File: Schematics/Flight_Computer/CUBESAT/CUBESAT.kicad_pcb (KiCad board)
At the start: 2 copper layers, 90 x 90 mm, 47 parts, among them J1 6 Pin Connector, J2 M22-6003005, J3 UFL, U1 ADXL345BCCZ, U2 NEO-M8N-0, U3 IAM-20380, U4 MAGNETOMETER, U5 STM32F446RET6, U6 LM75AIM_NOPB

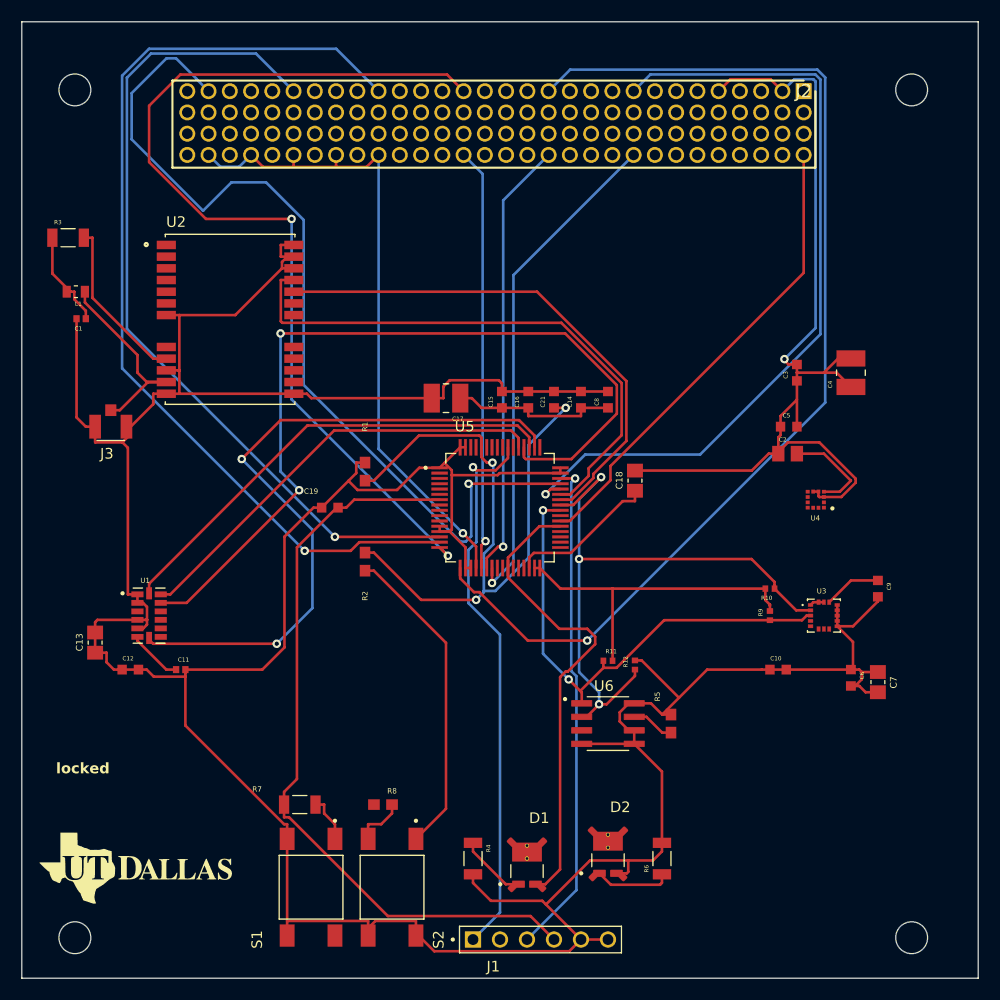
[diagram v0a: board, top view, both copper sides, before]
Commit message: updated pcb without traces or via's
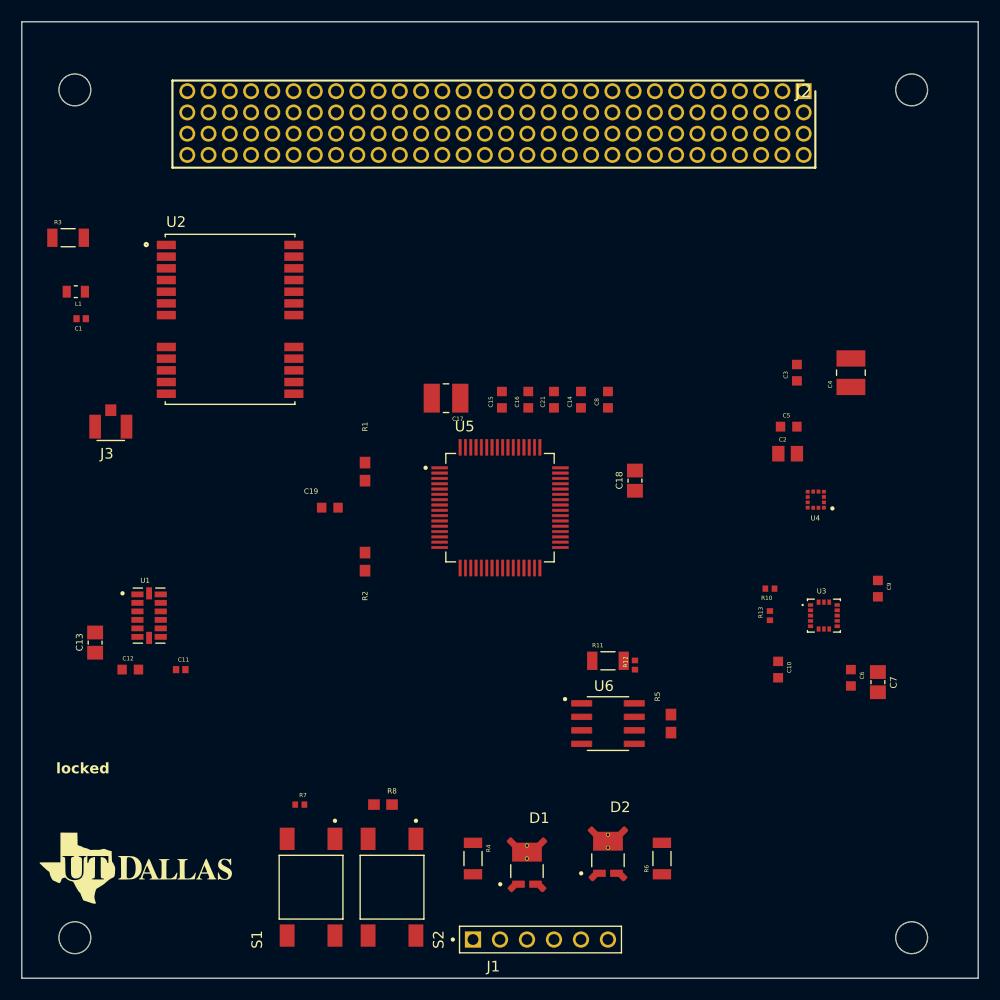
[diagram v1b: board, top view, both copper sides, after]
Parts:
- removed R9: ~, CUBESAT:Resistor4.7kO
- added R13: 4.7k, CUBESAT:Resistor4.7kO, F.Cu at (182.9, 104.1)
- J1: value 6 Pin Connector -> Conn_01x06_Pin
- J3: value UFL -> U.FL-R-SMT_01_
- R11: value 4.7k -> 100; footprint CUBESAT:Resistor4.7kO -> CUBESAT:Reistor100O
- R7: value 100 -> 4.7k; footprint CUBESAT:Reistor100O -> CUBESAT:Resistor4.7kO
- turned C10 to -90 degrees
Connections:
- C1 pad 2: 3.3 V -> GND
- C10 pad 1: 3.3 V -> GND
- C12 pad 2: 3.3 V -> GND
- C13 pad 2: 3.3 V -> GND
- C14 pad 1: Net-(C14-Pad1) -> 3.3 V
- C14 pad 2: 3.3 V -> GND
- C15 pad 1: Net-(C14-Pad1) -> 3.3 V
- C15 pad 2: 3.3 V -> GND
- C16 pad 1: Net-(C14-Pad1) -> 3.3 V
- C16 pad 2: 3.3 V -> GND
- C17 pad 1: Net-(C14-Pad1) -> 3.3 V
- C17 pad 2: 3.3 V -> GND
- C18 pad 1: Net-(U5-VCAP_1) -> GND
- C18 pad 2: 3.3 V -> Net-(U5-VCAP_1)
- C19 pad 2: 3.3 V -> GND
- C2 pad 1: 3.3 V -> GND
- C21 pad 1: BOOT0 -> GND
- C21 pad 2: 3.3 V -> BOOT0
- C3 pad 1: 3.3 V -> GND
- C4 pad 1: 3.3 V -> GND
- C5 pad 1: 3.3 V -> GND
- C6 pad 2: 3.3 V -> GND
- C7 pad 2: 3.3 V -> GND
- C8 pad 1: Net-(C14-Pad1) -> 3.3 V
- C8 pad 2: 3.3 V -> GND
- C9 pad 2: 3.3 V -> GND
- J1 pad 2: unconnected-(J1-Pad2) -> SWCLK
- J1 pad 6: 3.3 V -> GND
- J2 pad 2: 3.3 V -> GND
- J3 pad 1: 3.3 V -> GND
- J3 pad 2: 3.3 V -> GND
- R1 pad 1: 3.3 V -> GND
- R11 pad 1: I2C 3 SDA -> Net-(R11-Pad1)
- R11 pad 2: 3.3 V -> NRST
- R4 pad 2: 3.3 V -> GND
- R5 pad 1: Net-(U6-A0) -> 3.3 V
- R5 pad 2: 3.3 V -> Net-(U6-A0)
- R6 pad 2: 3.3 V -> GND
- R7 pad 1: NRST -> 3.3 V
- R7 pad 2: Net-(R7-Pad2) -> I2C 3 SCL
- R8 pad 1: 3.3 V -> GND
- S1 pad 1: Net-(R7-Pad2) -> Net-(R11-Pad1)
- S1 pad 2: 3.3 V -> GND
- S1 pad 4: 3.3 V -> GND
- S2 pad 4: 3.3 V -> unconnected-(S2-Pad4)
- U1 pad 2: 3.3 V -> GND
- U1 pad 4: 3.3 V -> GND
- U1 pad 5: 3.3 V -> GND
- U2 pad 10: 3.3 V -> GND
- U2 pad 12: 3.3 V -> GND
- U2 pad 13: 3.3 V -> GND
- U2 pad 24: 3.3 V -> GND
- U2 pad 7: 3.3 V -> GND
- U3 pad 10: 3.3 V -> GND
- U3 pad 11: 3.3 V -> GND
- U3 pad 12: 3.3 V -> GND
- U3 pad 13: 3.3 V -> GND
- U3 pad 15: 3.3 V -> GND
- U3 pad 7: 3.3 V -> GND
- U3 pad 9: 3.3 V -> GND
- U4 pad 3: 3.3 V -> GND
- U5 pad 12: 3.3 V -> GND
- U5 pad 18: 3.3 V -> GND
- U5 pad 31: 3.3 V -> GND
- U5 pad 47: 3.3 V -> GND
- U5 pad 63: 3.3 V -> GND
- U6 pad 4: 3.3 V -> GND
- U6 pad 5: 3.3 V -> GND
- U6 pad 6: 3.3 V -> GND
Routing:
- net 3.3 V: track 483.3 -> 0.00 mm, vias 1 -> 0
- net Phase Shifter 2: track 104.8 -> 0.00 mm, vias 1 -> 0
- net Phase Shifter 4: track 91.7 -> 0.00 mm, vias 1 -> 0
- net Phase Shifter 3: track 91.3 -> 0.00 mm, vias 2 -> 0
- net TRX: track 87.1 -> 0.00 mm, vias 1 -> 0
- net ADXL345 MISO: track 80.8 -> 0.00 mm, vias 2 -> 0
- net MODEM RESET: track 79.3 -> 0.00 mm, vias 1 -> 0
- net Phase Shifter 1: track 76.1 -> 0.00 mm, vias 1 -> 0
- net NRST: track 71.3 -> 0.00 mm
- net ADXL345 CS: track 64.6 -> 0.00 mm, vias 2 -> 0
- net BOOT0: track 64.0 -> 0.00 mm, vias 3 -> 0
- net CC1120 (NSS/CS): track 62.8 -> 0.00 mm, vias 1 -> 0
- net I2C 3 SCL: track 59.3 -> 0.00 mm, vias 3 -> 0
- net NEO-M8N-0 RXD: track 53.0 -> 0.00 mm
- net SWO: track 52.1 -> 0.00 mm, vias 1 -> 0
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
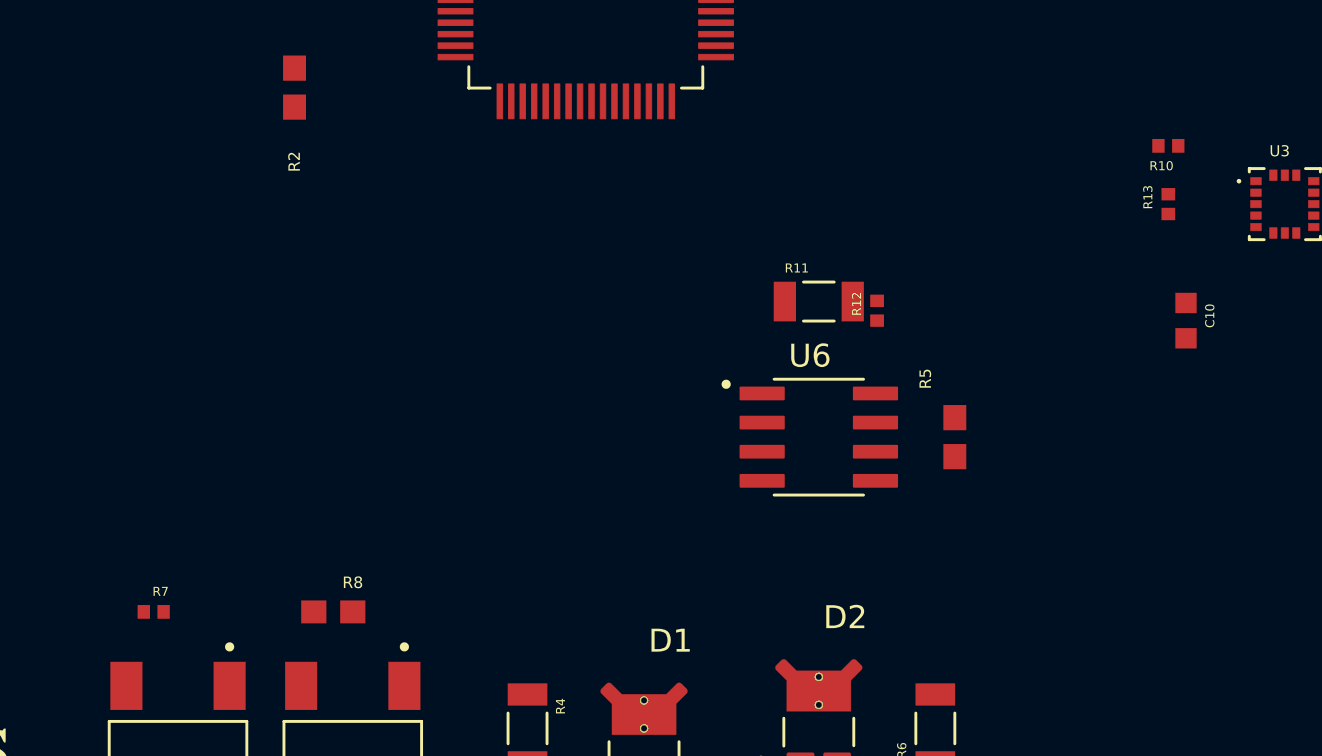
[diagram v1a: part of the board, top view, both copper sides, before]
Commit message: feat: add CC1120 drivers
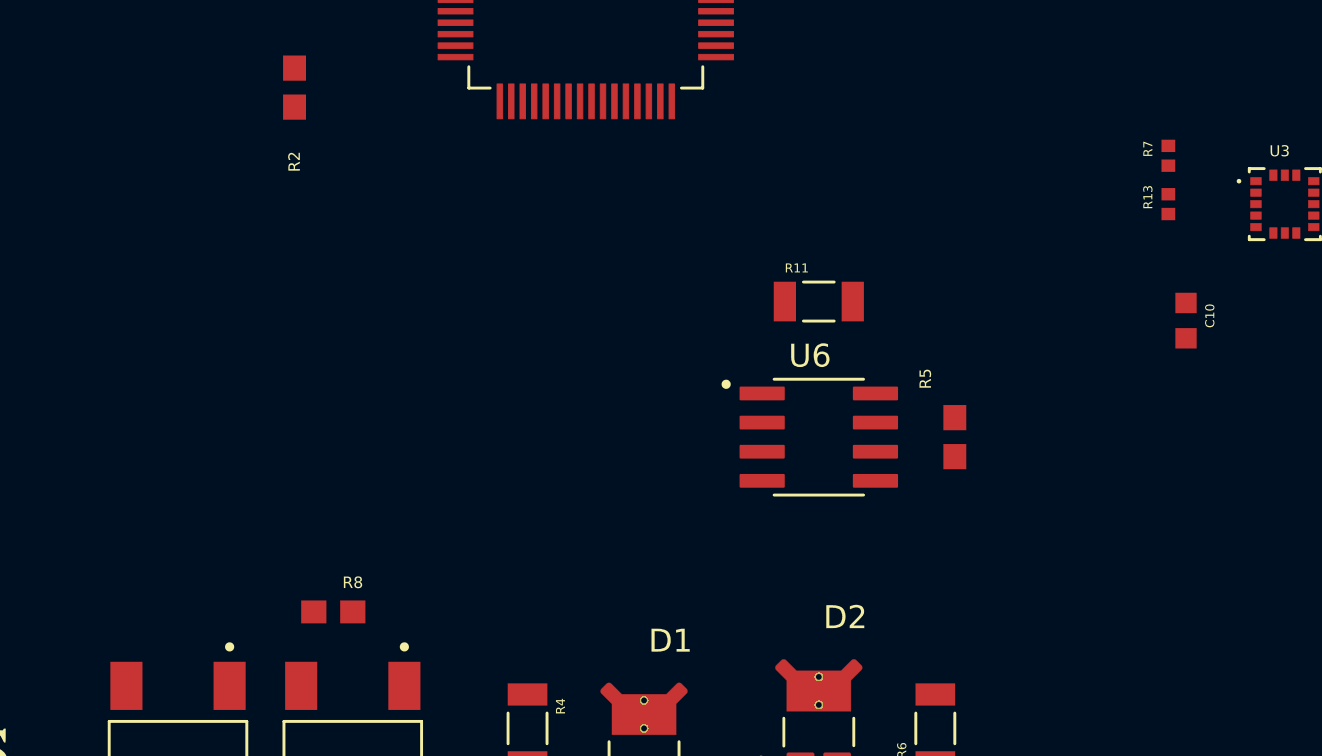
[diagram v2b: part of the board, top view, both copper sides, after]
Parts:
- removed R10: ~, CUBESAT:Resistor4.7kO
- removed R12: 4.7k, CUBESAT:Resistor4.7kO
- moved R7 48.5 mm to (182.9, 102.0), turned to 90 degrees
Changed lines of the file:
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@@
       (net 193 "unconnected-(S2-Pad4)") (pintype "passive") (solder_mask_margin 0.102))
-  )
-  (footprint "CUBESAT:Resistor4.7kO" (layer "F.Cu")
-    (at 182.88 101.6 180)
-    (property "AVAILABILITY" "")
-    (property "Availability" "")
-    (property "Check_prices" "")
-    (property "DESCRIPTION" "")
-    (property "Description" "\n4.7 kOhms ±1% 0.063W, 1/16W Chip Resistor 0402 (1005 Metric) Moisture Resistant Thick Film\n")
-    (property "MF" "")
-    (property "MP" "")
-    (property "PACKAGE" "")
-    (property "PRICE" "")
-    (property "PURCHASE-URL" "")
-    (property "Package" "")
-    (property "Price" "")
-    (property "Sheetfile" "CUBESAT.kicad_sch")
-    (property "Sheetname" "")
-    (property "SnapEDA_Link" "")
-    (attr smd)
-    (fp_text reference "R10" (at 0.3 -0.88) (layer "F.SilkS")
-        (effects (font (size 0.393701 0.393701) (thickness 0.15)))
-    )
-    (fp_text value "~" (at 2.05 0.88) (layer "F.Fab")
-        (effects (font (size 0.393701 0.393701) (thickness 0.15)))
-    )
-    (fp_line (start -0.95 -0.55) (end 0.95 -0.55)
-      (stroke (width 0.05) (type solid)) (layer "F.CrtYd"))
-    (fp_line (start -0.95 0.55) (end -0.95 -0.55)
-      (stroke (width 0.05) (type solid)) (layer "F.CrtYd"))
-    (fp_line (start -0.95 0.55) (end 0.95 0.55)
-      (stroke (width 0.05) (type solid)) (layer "F.CrtYd"))
-    (fp_line (start 0.95 0.55) (end 0.95 -0.55)
-      (stroke (width 0.05) (type solid)) (layer "F.CrtYd"))
-    (fp_line (start -0.53 0.28) (end -0.53 -0.28)
-      (stroke (width 0.127) (type solid)) (layer "F.Fab"))
-    (fp_line (start 0.53 -0.28) (end -0.53 -0.28)
-      (stroke (width 0.127) (type solid)) (layer "F.Fab"))
-    (fp_line (start 0.53 0.28) (end -0.53 0.28)
-      (stroke (width 0.127) (type solid)) (layer "F.Fab"))
-    (fp_line (start 0.53 0.28) (end 0.53 -0.28)
-      (stroke (width 0.127) (type solid)) (layer "F.Fab"))
-    (pad "1" smd rect (at -0.432 0 180) (size 0.54 0.6) (layers "F.Cu" "F.Paste" "F.Mask")
-      (net 136 "I2C 3 SCL") (pintype "passive") (solder_mask_margin 0.102))
-    (pad "2" smd rect (at 0.432 0 180) (size 0.54 0.6) (layers "F.Cu" "F.Paste" "F.Mask")
-      (net 1 "3.3 V") (pintype "passive") (solder_mask_margin 0.102))
   )
   (footprint "CUBESAT:Capacitor100nf" (layer "F.Cu")
@@
   )
   (footprint "CUBESAT:Resistor4.7kO" (layer "F.Cu")
-    (at 170.18 108.788 90)
-    (property "AVAILABILITY" "")
-    (property "Availability" "")
-    (property "Check_prices" "")
-    (property "DESCRIPTION" "")
-    (property "Description" "\n4.7 kOhms ±1% 0.063W, 1/16W Chip Resistor 0402 (1005 Metric) Moisture Resistant Thick Film\n")
-    (property "MF" "")
-    (property "MP" "")
-    (property "PACKAGE" "")
-    (property "PRICE" "")
-    (property "PURCHASE-URL" "")
-    (property "Package" "")
-    (property "Price" "")
+    (at 182.88 102.032 90)
     (property "Sheetfile" "CUBESAT.kicad_sch")
     (property "Sheetname" "")
-    (property "SnapEDA_Link" "")
+    (property "ki_description" "Resistor")
+    (property "ki_keywords" "R res resistor")
     (attr smd)
-    (fp_text reference "R12" (at 0.3 -0.88 90) (layer "F.SilkS")
+    (fp_text reference "R7" (at 0.3 -0.88 90) (layer "F.SilkS")
         (effects (font (size 0.393701 0.393701) (thickness 0.15)))
     )
-    (fp_text value "4.7k" (at -0.432 0.88 90) (layer "F.Fab")
-        (effects (font (size 0.393701 0.393701) (thickness 0.098425)))
+    (fp_text value "4.7k" (at 2.05 0.88 90) (layer "F.Fab")
+        (effects (font (size 0.393701 0.393701) (thickness 0.15)))
     )
     (fp_line (start -0.95 -0.55) (end 0.95 -0.55)
@@
       (stroke (width 0.127) (type solid)) (layer "F.Fab"))
     (pad "1" smd rect (at -0.432 0 90) (size 0.54 0.6) (layers "F.Cu" "F.Paste" "F.Mask")
-      (net 136 "I2C 3 SCL") (pintype "passive") (solder_mask_margin 0.102))
+      (net 1 "3.3 V") (pintype "passive") (solder_mask_margin 0.102))
     (pad "2" smd rect (at 0.432 0 90) (size 0.54 0.6) (layers "F.Cu" "F.Paste" "F.Mask")
-      (net 1 "3.3 V") (pintype "passive") (solder_mask_margin 0.102))
-  )
-  (footprint "CUBESAT:Resistor4.7kO" (layer "F.Cu")
-    (at 138.64 121.92)
-    (property "Sheetfile" "CUBESAT.kicad_sch")
-    (property "Sheetname" "")
-    (property "ki_description" "Resistor")
-    (property "ki_keywords" "R res resistor")
-    (attr smd)
-    (fp_text reference "R7" (at 0.3 -0.88) (layer "F.SilkS")
-        (effects (font (size 0.393701 0.393701) (thickness 0.15)))
-    )
-    (fp_text value "4.7k" (at 2.05 0.88) (layer "F.Fab")
-        (effects (font (size 0.393701 0.393701) (thickness 0.15)))
-    )
-    (fp_line (start -0.95 -0.55) (end 0.95 -0.55)
-      (stroke (width 0.05) (type solid)) (layer "F.CrtYd"))
-    (fp_line (start -0.95 0.55) (end -0.95 -0.55)
-      (stroke (width 0.05) (type solid)) (layer "F.CrtYd"))
-    (fp_line (start -0.95 0.55) (end 0.95 0.55)
-      (stroke (width 0.05) (type solid)) (layer "F.CrtYd"))
-    (fp_line (start 0.95 0.55) (end 0.95 -0.55)
-      (stroke (width 0.05) (type solid)) (layer "F.CrtYd"))
-    (fp_line (start -0.53 0.28) (end -0.53 -0.28)
-      (stroke (width 0.127) (type solid)) (layer "F.Fab"))
-    (fp_line (start 0.53 -0.28) (end -0.53 -0.28)
-      (stroke (width 0.127) (type solid)) (layer "F.Fab"))
-    (fp_line (start 0.53 0.28) (end -0.53 0.28)
-      (stroke (width 0.127) (type solid)) (layer "F.Fab"))
-    (fp_line (start 0.53 0.28) (end 0.53 -0.28)
-      (stroke (width 0.127) (type solid)) (layer "F.Fab"))
-    (pad "1" smd rect (at -0.432 0) (size 0.54 0.6) (layers "F.Cu" "F.Paste" "F.Mask")
-      (net 1 "3.3 V") (pintype "passive") (solder_mask_margin 0.102))
-    (pad "2" smd rect (at 0.432 0) (size 0.54 0.6) (layers "F.Cu" "F.Paste" "F.Mask")
       (net 136 "I2C 3 SCL") (pintype "passive") (solder_mask_margin 0.102))
   )
